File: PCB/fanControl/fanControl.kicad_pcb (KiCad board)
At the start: 2 copper layers, 73.2 x 38 mm, 81 parts, among them J1 USB_B_Micro, J2 Barrel_Jack_Switch, J3 Conn_01x03, J4 Conn_01x06, J5 Conn_01x04, Q1 PNM723, Q2 FDD4243, Q3 BC547, Q4 PNM723, Q5 BC847BDW1, Q6 SI2324A, U1 DS18B20, U2 CH340B, U3 LM2575BT-ADJ, U4 ESP-12E, U5 LD1117S33CTR, Y1 12M

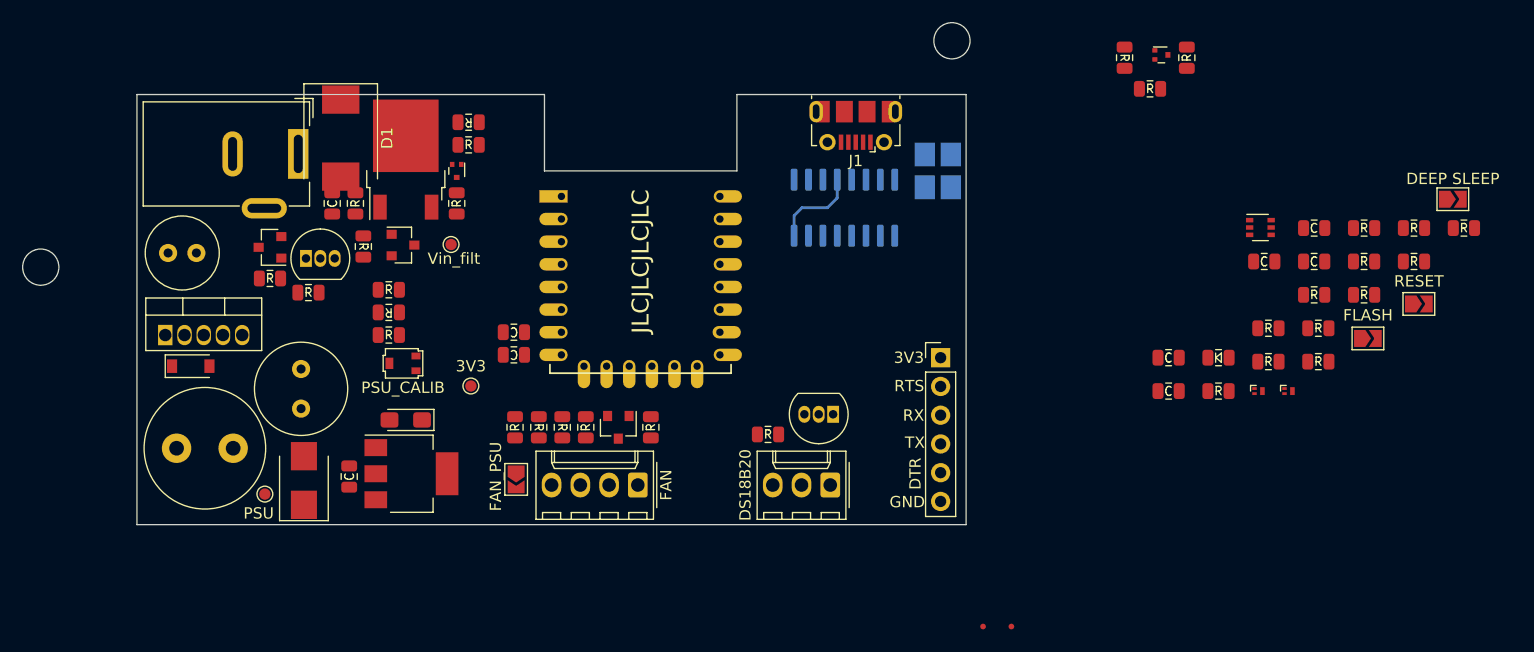
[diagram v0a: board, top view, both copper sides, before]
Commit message: KiCad 6 migration
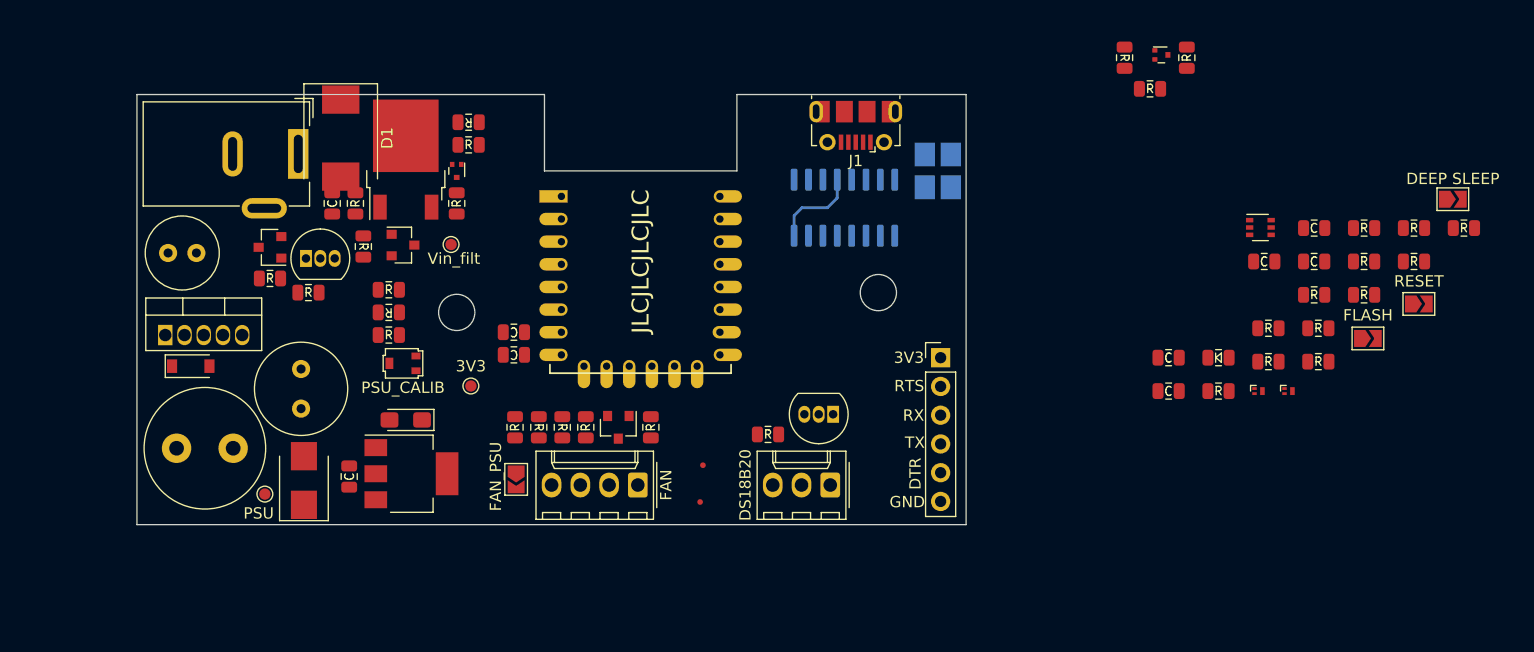
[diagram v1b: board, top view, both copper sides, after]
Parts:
- moved H1 37.0 mm to (171.2, 76.2)
- moved FID2 29.6 mm to (192.8, 93.0)
- moved FID1 28.6 mm to (193.0, 89.8)
- moved H2 23.2 mm to (208.5, 74.5)
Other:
- net class Default removed

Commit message: LCSC BOM done
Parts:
- removed R1, R18, R27, R28, R30, R8: 1k, agro-footprint:RES_0805
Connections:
- J1 pad 4: (no net) -> unconnected-(J1-Pad4)
- U2 pad 10: (no net) -> unconnected-(U2-Pad10)
- U2 pad 11: (no net) -> unconnected-(U2-Pad11)
- U2 pad 12: (no net) -> unconnected-(U2-Pad12)
- U2 pad 15: (no net) -> unconnected-(U2-Pad15)
- U2 pad 9: (no net) -> unconnected-(U2-Pad9)
- U4 pad 17: (no net) -> unconnected-(U4-Pad17)
- U4 pad 18: (no net) -> unconnected-(U4-Pad18)
- U4 pad 19: (no net) -> unconnected-(U4-Pad19)
- U4 pad 20: (no net) -> unconnected-(U4-Pad20)
- U4 pad 21: (no net) -> unconnected-(U4-Pad21)
- U4 pad 22: (no net) -> unconnected-(U4-Pad22)

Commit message: ver2
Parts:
- removed the C4 at (234.1, 80.2)
- removed the R12 at (251.4, 68.8)
- removed the R19 at (260.2, 68.8)
- removed the R7 at (163.0, 70.4)
- added C13: 10n 50V, agro-footprint:CAP_0805, F.Cu at (163.3, 68.2)
- added C14: 10n 50V, agro-footprint:CAP_0805, F.Cu at (206.7, 69.3)
- added C3: 22p, agro-footprint:CAP_0805, B.Cu at (212.9, 64.9)
- added D9: CUS10S30, Diode_SMD:D_SOD-323_HandSoldering, F.Cu at (155.1, 92.8)
- added FID2: Fiducial, Fiducial:Fiducial_0.5mm_Mask1.5mm, B.Cu at (197.3, 89.9)
- added FID4: Fiducial, Fiducial:Fiducial_0.5mm_Mask1.5mm, B.Cu at (151.5, 69.5)
- added H3: ToolingHole, fanControl:JLC_toolinghole, F.Cu at (213.2, 58.9)
- added H4: ToolingHole, fanControl:JLC_toolinghole, F.Cu at (148.9, 85.3)
- added JP1: SolderJumper_2_Open, Jumper:SolderJumper-2_P1.3mm_Open_TrianglePad1.0x1.5mm, B.Cu at (145.0, 59.8)
- added Q7: BC847B, Package_TO_SOT_SMD:SOT-23, F.Cu at (167.8, 62.5)
- added Q8: BSS84, Package_TO_SOT_SMD:SOT-23, F.Cu at (210.4, 70.1)
- added Q9: BC847B, Package_TO_SOT_SMD:SOT-23, B.Cu at (205.3, 77.4)
- added R14: 1k, agro-footprint:RES_0805, F.Cu at (200.1, 68.3)
- added R16: 100k, agro-footprint:RES_0805, F.Cu at (213.3, 70.1)
- added R17: 3k6, agro-footprint:RES_0805, F.Cu at (202.0, 68.3)
- added R2: 1k, agro-footprint:RES_0805, F.Cu at (168.8, 59.1)
- added R27: 470R, agro-footprint:RES_0805, B.Cu at (182.2, 70.8)
- added R28: 470R, agro-footprint:RES_0805, F.Cu at (171.9, 68.5)
- added R29: 1k, agro-footprint:RES_0805, F.Cu at (187.3, 85.5)
- added R3: 100k, agro-footprint:RES_0805, F.Cu at (170.8, 58.8)
- added R32: 1k, agro-footprint:RES_0805, F.Cu at (185.1, 85.5)
- added R33: 100k, agro-footprint:RES_0805, F.Cu at (180.6, 85.5)
- added R34: 10k, agro-footprint:RES_0805, F.Cu at (155.1, 89.0)
- added R35: 100k, agro-footprint:RES_0805, F.Cu at (166.8, 59.1)
- added R36: 6k8, agro-footprint:RES_0805, F.Cu at (203.9, 68.3)
- added R8: 10k, agro-footprint:RES_0805, F.Cu at (161.8, 74.5)
- added TP4: TestPoint, TestPoint:TestPoint_Pad_D1.0mm, F.Cu at (205.0, 64.2)
- added TP5: TestPoint, TestPoint:TestPoint_Pad_D1.0mm, F.Cu at (209.6, 64.2)
- C1: renamed from C3; moved to B.Cu
- C10: value 100n -> 10u 10V; footprint agro-footprint:CAP_0805 -> Capacitor_Tantalum_SMD:CP_EIA-3216-18_Kemet-A_Pad1.58x1.35mm_HandSolder
- C12: value 10u -> 10u 10V
- C2: renamed from C1; value 10n -> 10n 50V; moved to B.Cu
- C5, C6, C7, D2, D4, D8, R11, R21, R22, R23: moved to B.Cu
- C9: footprint agro-footprint:CAP_0805 -> Capacitor_SMD:C_1206_3216Metric
- D3, D5: value BZT52C3V3LP -> BZX84C3V6; footprint Package_DFN_QFN:Diodes_DFN1006-3 -> Diode_SMD:D_SOT-23_ANK
- D7: value MBRS140 -> 10BQ015
- J2: footprint fanControl:BarrelJack_Wuerth_6941xx301002 -> Connector_BarrelJack:BarrelJack_GCT_DCJ200-10-A_Horizontal
- Q1: value PNM723 -> FDD4243; footprint Package_TO_SOT_SMD:SOT-723 -> Package_TO_SOT_SMD:TO-252-2; moved to B.Cu
- Q2: value FDD4243 -> BSS84; footprint fanControl:TO-252-2_TabPin5 -> Package_TO_SOT_SMD:SOT-23
- Q3, U1: footprint Package_TO_SOT_THT:TO-92_Inline -> Package_TO_SOT_THT:TO-92_Inline_Wide
- Q4: value PNM723 -> BC847B; footprint Package_TO_SOT_SMD:SOT-723 -> Package_TO_SOT_SMD:SOT-23; moved to B.Cu
- Q5: value BC847BDW1 -> BC847B; footprint Package_TO_SOT_SMD:SOT-363_SC-70-6 -> Package_TO_SOT_SMD:SOT-23
- Q6: value SI2324A -> BRCS4484; footprint Package_TO_SOT_SMD:SOT-23 -> fanControl:BRCS4484
- R1: renamed from R4; moved to B.Cu
- R10: value 6k8 -> 10k; moved to B.Cu
- R12: renamed from R14; moved to B.Cu
- R13: value 10k -> 470R; moved to B.Cu
- R15: value 470R -> 100k
- R20, R31: value 10k -> 1k
- R24, R25: value 470R -> 10k; moved to B.Cu
- R5: renamed from R3; value 2k -> 1k1
- RV1: value R_POT_TRIM -> 1k; footprint fanControl:BournsTC42X -> fanControl:pot
- U4: renamed from U5; value LD1117S33CTR -> LM1117
- U5: renamed from U4; footprint kicad-ESP8266:ESP-12E -> ESP8266:ESP-12E
- Y1: footprint Crystal:Crystal_SMD_3225-4Pin_3.2x2.5mm_HandSoldering -> Crystal:Crystal_SMD_3225-4Pin_3.2x2.5mm
- moved R20 92.8 mm to (163.5, 81.0), turned to 180 degrees
- moved JP4 87.5 mm to (171.9, 72.1), turned to 180 degrees
- moved JP5 84.4 mm to (171.9, 74.6), turned to 180 degrees
- moved D3 78.8 mm to (167.8, 66.0)
- moved R24 77.0 mm to (178.8, 66.7), turned to 90 degrees
- moved R23 64.4 mm to (179.5, 69.8), turned to 180 degrees
- moved R22 63.9 mm to (187.5, 75.2)
- moved R25 63.5 mm to (188.2, 78.0), turned to 90 degrees
- moved R21 60.1 mm to (187.5, 73.2)
- moved D8 59.7 mm to (179.5, 71.8)
- moved JP3 56.8 mm to (195.0, 79.4), turned to 180 degrees
- moved R12 49.9 mm to (200.6, 63.2), turned to 180 degrees
- moved R26 48.0 mm to (195.0, 77.2), turned to 180 degrees
- moved R15 47.0 mm to (200.1, 71.8), turned to -90 degrees
- moved R13 43.9 mm to (200.6, 61.2), turned to 180 degrees
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- renumbered C2 to C4, FID2 to FID3, JP1 to JP2, JP2 to JP3, JP3 to JP4, JP4 to JP5, R16 to R18, R17 to R19, R29 to R30, R2 to R4, R5 to R6, R6 to R7
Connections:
- net Net-(C3-Pad2) renamed /XTAL_N
- net Net-(C4-Pad1) renamed /XTAL_P
- C10 pad 1: /3V3 -> Net-(C10-Pad1)
- C11 pad 1: /PSU -> /3V3
- C2 pad 1: Net-(C1-Pad1) -> Net-(C2-Pad1)
- D2 pad 2: Net-(C1-Pad1) -> Net-(C2-Pad1)
- D7 pad 1: /PSU -> Net-(C10-Pad1)
- J4 pad 1: /3V3 -> /GPIO0
- J4 pad 2: /nRST -> /TXD0
- J4 pad 3: /RX -> /RXD0
- J4 pad 4: /TX -> /3V3
- J4 pad 5: /GPIO0 -> /nRST
- JP3 pad 1: Net-(JP2-Pad1) -> Net-(JP3-Pad1)
- JP4 pad 2: Net-(JP3-Pad2) -> Net-(JP4-Pad2)
- JP5 pad 1: Net-(JP3-Pad2) -> GND
- JP5 pad 2: GND -> Net-(JP4-Pad2)
- Q1 pad 1: Net-(Q1-Pad1) -> Net-(C2-Pad1)
- Q1 pad 2: Net-(Q1-Pad2) -> /Vin
- Q2 pad 1: /Vin_filt -> Net-(Q2-Pad1)
- Q4 pad 1: Net-(Q4-Pad1) -> Net-(R10-Pad2)
- Q4 pad 2: Net-(Q4-Pad2) -> Net-(R11-Pad2)
- Q4 pad 3: /USB_5V -> /nRST
- Q5 pad 1: Net-(Q5-Pad1) -> Net-(R14-Pad2)
- Q5 pad 2: Net-(Q5-Pad2) -> GND
- Q5 pad 3: /GPIO0 -> Net-(Q5-Pad3)
- R1 pad 1: Net-(C1-Pad1) -> Net-(C2-Pad1)
- R10 pad 1: Net-(Q4-Pad2) -> Net-(R10-Pad1)
- R10 pad 2: /USB_sense -> Net-(R10-Pad2)
- R11 pad 1: /USB_sense -> Net-(R11-Pad1)
- R11 pad 2: GND -> Net-(R11-Pad2)
- R12 pad 2: /TX -> /RXD0
- R13 pad 1: Net-(Q5-Pad5) -> Net-(R13-Pad1)
- R13 pad 2: Net-(Q5-Pad1) -> /TXD0
- R15 pad 1: /RX -> Net-(R14-Pad2)
- R15 pad 2: Net-(R15-Pad2) -> GND
- R19 pad 1: Net-(R17-Pad1) -> Net-(R19-Pad1)
- R20 pad 1: /3V3 -> Net-(R19-Pad1)
- R20 pad 2: /GPIO2 -> /PSU
- R21 pad 2: /EN -> /GPIO0
- R22 pad 2: /nRST -> /GPIO2
- R23 pad 1: GND -> /3V3
- R23 pad 2: /GPIO15 -> /EN
- R24 pad 1: /GPIO0 -> /3V3
- R24 pad 2: Net-(JP2-Pad1) -> /nRST
- R25 pad 1: /3V3 -> GND
- R25 pad 2: Net-(D8-Pad2) -> /GPIO15
- R26 pad 1: /nRST -> Net-(JP3-Pad1)
- R26 pad 2: Net-(JP3-Pad2) -> /GPIO0
- R31 pad 1: /PWM -> /PWMpin
- R31 pad 2: GND -> /PWM
- R4 pad 1: Net-(Q1-Pad2) -> Net-(Q2-Pad3)
- RV1 pad 2: Net-(R17-Pad1) -> Net-(R19-Pad1)
- RV1 pad 3: Net-(R17-Pad1) -> Net-(R19-Pad1)
- U2 pad 13: Net-(Q5-Pad4) -> Net-(R10-Pad1)
- U2 pad 14: Net-(Q5-Pad1) -> Net-(R11-Pad2)
- U2 pad 3: Net-(R15-Pad2) -> Net-(R13-Pad1)
- U4 pad 3: /PSU -> Net-(C10-Pad1)
- U5 pad 15: /TX -> /RXD0
- U5 pad 16: /RX -> /TXD0
- U5 pad 5: /RPM -> /POW_EN
- U5 pad 6: /POW_EN -> /RPM
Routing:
- net /3V3: track 7.85 -> 138.9 mm
- net GND: track 0.00 -> 127.7 mm, vias 0 -> 3
- net /PSU: track 0.00 -> 121.1 mm, vias 0 -> 6
- net /Vin_filt: track 0.00 -> 113.8 mm, vias 0 -> 3
- net /GPIO0: track 0.00 -> 46.7 mm, vias 0 -> 1
- net /oneWire: track 0.00 -> 41.9 mm
- net /nRST: track 0.00 -> 37.2 mm, vias 0 -> 1
- net /Vin: track 0.00 -> 28.5 mm
- net /V_MON: track 0.00 -> 25.6 mm
- net /USB_sense: track 0.00 -> 22.9 mm
- net /RPM: track 0.00 -> 21.9 mm
- net Net-(C2-Pad1): track 0.00 -> 21.6 mm
- net /FAN_POW: track 0.00 -> 20.2 mm
- net /POW_EN: track 0.00 -> 16.7 mm
- net Net-(Q8-Pad3): track 0.00 -> 13.9 mm
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- added copper zone on B.Cu, net GND
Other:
- board size 73.2 x 38 mm -> 72.8 x 38 mm
- board text added: "4 pin fan controller"
- board text added: "BakaBoard"

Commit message: before optocouplers
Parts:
- added R37: 1k, agro-footprint:RES_0805, F.Cu at (202.7, 73.6)
- added R38: 10k, agro-footprint:RES_0805, F.Cu at (168.8, 59.0)
- D3: value BZX84C3V6 -> BZX84C3V3; moved to B.Cu
- D5: value BZX84C3V6 -> BZX84C3V3
- R10, R11: value 10k -> 4k7
- R14, R2: value 1k -> 22k
- R15, R16, R35: value 100k -> 10k
- R17: value 3k6 -> 4k7
- R3: value 100k -> 1k
- R4: value 6k8 -> 22k
- R5: value 1k1 -> 3k3
- moved D3 11.8 mm to (179.5, 67.0), turned to 90 degrees
- moved C13 8.45 mm to (171.4, 65.8)
- moved R16 8.22 mm to (205.8, 66.7), turned to 180 degrees
- moved R3 7.88 mm to (168.7, 66.4)
- moved R2 7.62 mm to (166.7, 66.4), turned to 90 degrees
- moved R17 7.59 mm to (209.4, 66.7), turned to 0 degrees
- moved R36 6.00 mm to (209.4, 70.7), turned to 0 degrees
- moved Q9 5.30 mm to (208.9, 73.5)
- moved Q8 4.58 mm to (205.8, 69.7), turned to -90 degrees
- moved C3 3.80 mm to (212.9, 61.1)
- moved C1 3.80 mm to (212.9, 67.3)
- moved Y1 3.80 mm to (212.9, 64.2)
- moved R11 3.67 mm to (205.9, 76.3), turned to 0 degrees
- moved R24 3.51 mm to (182.3, 67.0)
- moved Q2 3.30 mm to (171.8, 59.0)
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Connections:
- Q4 pad 2: Net-(R11-Pad2) -> Net-(Q4-Pad2)
- Q5 pad 1: Net-(R14-Pad2) -> Net-(Q5-Pad1)
- Q5 pad 2: GND -> Net-(Q5-Pad2)
- Q7 pad 2: GND -> Net-(Q7-Pad2)
- Q9 pad 1: Net-(R11-Pad1) -> Net-(Q9-Pad1)
- R11 pad 1: Net-(R11-Pad1) -> Net-(Q4-Pad2)
- R11 pad 2: Net-(R11-Pad2) -> Net-(Q9-Pad1)
- R14 pad 2: Net-(R14-Pad2) -> Net-(Q5-Pad1)
- R15 pad 1: Net-(R14-Pad2) -> GND
- R15 pad 2: GND -> Net-(Q5-Pad1)
- R3 pad 1: Net-(Q2-Pad1) -> Net-(Q7-Pad2)
- R3 pad 2: /Vin_filt -> GND
- R36 pad 1: /USB_sense -> GND
- R36 pad 2: GND -> /USB_sense
- R5 pad 1: /V_MON -> GND
- R5 pad 2: GND -> /V_MON
- U2 pad 14: Net-(R11-Pad2) -> Net-(Q4-Pad2)
- U5 pad 5: /POW_EN -> /PWMpin
- U5 pad 6: /RPM -> /POW_EN
- U5 pad 7: /PWMpin -> /RPM
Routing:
- net GND: track 127.7 -> 158.5 mm
- net /V_MON: track 25.6 -> 13.0 mm
- net /PSU: track 121.1 -> 110.9 mm, vias 6 -> 5
- net /3V3: track 138.9 -> 148.7 mm
- net /PWMpin: track 10.8 -> 19.9 mm
- net Net-(Q8-Pad3): track 13.9 -> 5.28 mm
- net /USB_sense: track 22.9 -> 30.6 mm
- net Net-(Q4-Pad2): track 0.00 -> 7.70 mm
- net Net-(R11-Pad2): track 7.10 -> 0.00 mm
- net /GPIO0: track 46.7 -> 52.5 mm
- net Net-(Q5-Pad1): track 0.00 -> 4.56 mm
- net Net-(R14-Pad2): track 3.57 -> 0.00 mm
- net Net-(Q9-Pad2): track 8.10 -> 4.58 mm
- net Net-(Q5-Pad3): track 11.8 -> 8.40 mm
- net Net-(Q5-Pad2): track 0.00 -> 2.81 mm
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
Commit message: RFQ2
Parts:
- added Q10: BC847B, Package_TO_SOT_SMD:SOT-23, F.Cu at (194.9, 92.5)
- added R39: 10k, agro-footprint:RES_0805, F.Cu at (187.3, 85.5)
- added R40: 22k, agro-footprint:RES_0805, F.Cu at (195.9, 89.0)
- Q6: value BRCS4484 -> DMP4065; footprint fanControl:BRCS4484 -> Package_TO_SOT_SMD:SOT-23
- R16: value 10k -> 3k3
- R17: value 4k7 -> 3k3
- R18: value 1k1 1% -> 1k1
- R19: value 3k3 1% -> 3k3
- R30: value 100k -> 10k
- moved R29 8.33 mm to (191.9, 92.5), turned to 90 degrees
- moved Q6 1.57 mm to (192.9, 89.0), turned to 180 degrees
- moved R9 0.50 mm to (154.1, 72.5)
- moved TP1 0.27 mm to (194.7, 85.5)
- moved Q3 0.20 mm to (157.2, 71.5)
- moved D1 0.20 mm to (162.2, 62.2)
- moved R12 0.11 mm to (200.6, 63.1), turned to 0 degrees
- moved R30 0.09 mm to (189.5, 85.5), turned to -90 degrees
- turned R13 to 0 degrees
- turned R17 to 180 degrees
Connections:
- Q8 pad 3: Net-(Q8-Pad3) -> Net-(R17-Pad2)
- R12 pad 1: Net-(R12-Pad1) -> /RXD0
- R12 pad 2: /RXD0 -> Net-(R12-Pad2)
- R13 pad 1: Net-(R13-Pad1) -> /TXD0
- R13 pad 2: /TXD0 -> Net-(R13-Pad2)
- R17 pad 1: Net-(Q8-Pad3) -> /USB_sense
- R17 pad 2: /USB_sense -> Net-(R17-Pad2)
- R29 pad 1: /POW_EN -> Net-(R29-Pad1)
- R29 pad 2: Net-(Q6-Pad1) -> GND
- R30 pad 1: Net-(Q6-Pad1) -> GND
- R30 pad 2: GND -> Net-(R30-Pad2)
- U2 pad 2: Net-(R12-Pad1) -> Net-(R12-Pad2)
- U2 pad 3: Net-(R13-Pad1) -> Net-(R13-Pad2)
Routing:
- net Net-(R30-Pad2): track 0.00 -> 10.2 mm
- net Net-(Q6-Pad1): track 11.8 -> 4.64 mm
- net Net-(R13-Pad2): track 0.00 -> 5.63 mm
- net Net-(R13-Pad1): track 5.63 -> 0.00 mm
- net Net-(R17-Pad2): track 0.00 -> 5.60 mm
- net Net-(Q8-Pad3): track 5.28 -> 0.00 mm
- net Net-(R12-Pad2): track 0.00 -> 2.83 mm
- net Net-(R12-Pad1): track 2.83 -> 0.00 mm
- net /FAN_POW: track 20.2 -> 18.0 mm
- net Net-(R29-Pad1): track 0.00 -> 2.07 mm
- net GND: track 158.5 -> 160.4 mm
- net /Vin: track 28.5 -> 27.0 mm
- net /Vin_filt: track 113.0 -> 112.1 mm
